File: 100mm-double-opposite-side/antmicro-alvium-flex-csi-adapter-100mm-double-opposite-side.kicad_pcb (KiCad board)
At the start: 2 copper layers, 81.8 x 100.1 mm, 3 parts, among them J1 WE_687622100002_FLEX, J2 WE_687622100002_FLEX, J3 WE_687650100002_FLEX

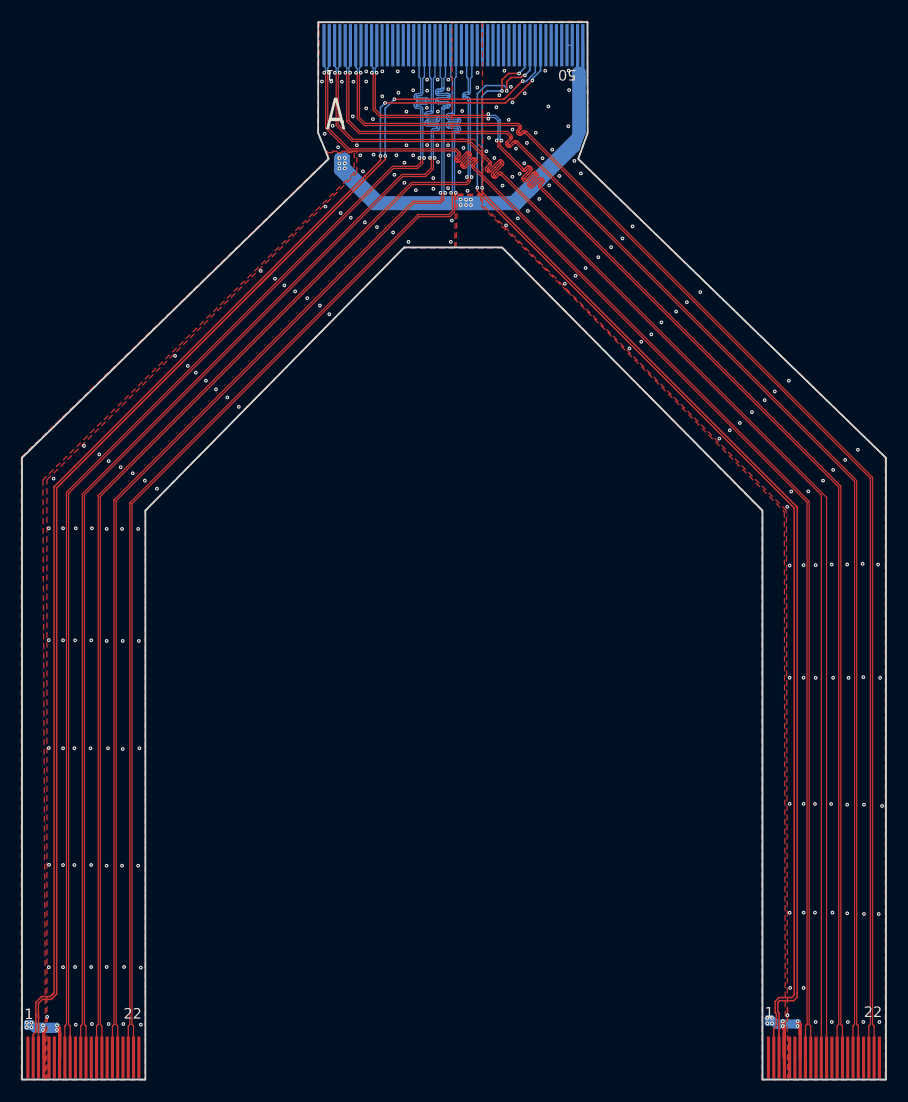
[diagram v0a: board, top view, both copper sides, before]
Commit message: 100mm-double-opposite: tweak polygon pours
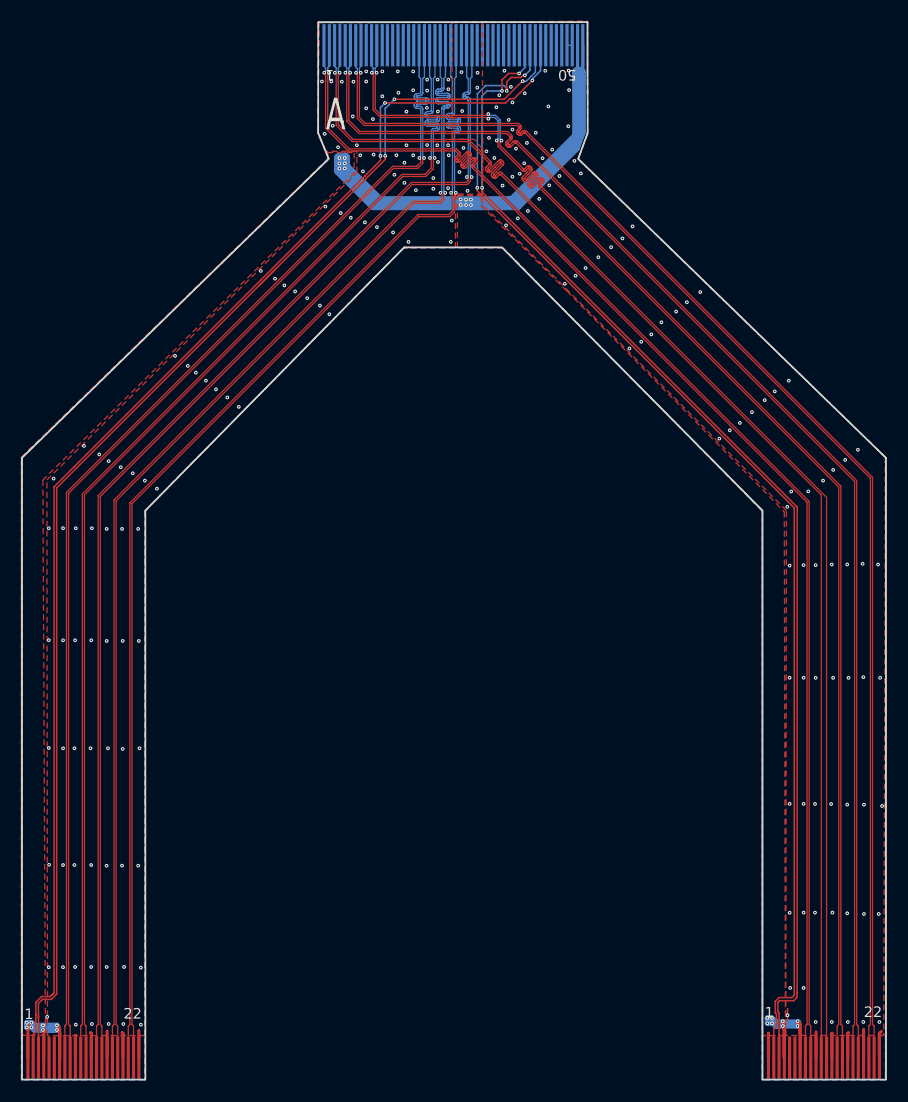
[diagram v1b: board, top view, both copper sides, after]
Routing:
- net /F1_GND: track 1.53 -> 25.9 mm
- net /F1_5V: track 115.4 -> 120.8 mm
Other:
- board text added: "Stiffener TOP"
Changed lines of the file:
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@@
-(kicad_pcb (version 20171130) (host pcbnew 5.1.6)
+(kicad_pcb (version 20171130) (host pcbnew 5.1.5+dfsg1-2~bpo10+1)
   (general
     (thickness 1.6)
     (drawings 73)
-    (tracks 1988)
+    (tracks 2008)
     (zones 0)
     (modules 3)
@@
   (page A4)
   (layers
-    (0 F.Cu signal)
-    (31 B.Cu signal)
+    (0 F.Cu signal hide)
+    (31 B.Cu signal hide)
     (32 B.Adhes user hide)
     (33 F.Adhes user hide)
     (34 B.Paste user hide)
     (35 F.Paste user hide)
-    (36 B.SilkS user)
-    (37 F.SilkS user)
+    (36 B.SilkS user hide)
+    (37 F.SilkS user hide)
     (38 B.Mask user hide)
     (39 F.Mask user hide)
-    (40 Dwgs.User user)
-    (41 Cmts.User user)
-    (42 Eco1.User user)
-    (43 Eco2.User user)
+    (40 Dwgs.User user hide)
+    (41 Cmts.User user hide)
+    (42 Eco1.User user hide)
+    (43 Eco2.User user hide)
     (44 Edge.Cuts user)
-    (45 Margin user)
-    (46 B.CrtYd user)
-    (47 F.CrtYd user)
-    (48 B.Fab user)
+    (45 Margin user hide)
+    (46 B.CrtYd user hide)
+    (47 F.CrtYd user hide)
+    (48 B.Fab user hide)
     (49 F.Fab user)
   )
   (setup
-    (last_trace_width 0.1)
+    (last_trace_width 0.3)
     (user_trace_width 0.1)
     (user_trace_width 0.15)
@@
   (gr_line (start 152.313 118.802) (end 163.997 118.802) (layer B.Fab) (width 0.15))
   (gr_line (start 82.209 111.662) (end 93.893 111.662) (layer B.Fab) (width 0.15))
-  (gr_text "Stiffener BOTTOM" (at 102.57 24.662) (layer B.Fab)
+  (gr_text "Stiffener TOP" (at 123.56 21.41) (layer F.Fab)
     (effects (font (size 1 1) (thickness 0.15)))
   )
@@
   (segment (start 154.686 112.164) (end 154.686 112.776) (width 0.15) (layer F.Cu) (net 1))
   (segment (start 154.7 112.15) (end 154.686 112.164) (width 0.15) (layer F.Cu) (net 1))
+  (segment (start 87.2824 114.689198) (end 87.29 114.681598) (width 0.3) (layer F.Cu) (net 1))
+  (segment (start 87.2824 116.7892) (end 87.2824 114.689198) (width 0.3) (layer F.Cu) (net 1))
+  (segment (start 88.7824 114.4892) (end 88.71 114.4168) (width 0.3) (layer F.Cu) (net 1))
+  (segment (start 88.7824 116.7892) (end 88.7824 114.4892) (width 0.3) (layer F.Cu) (net 1))
+  (segment (start 90.2824 116.7892) (end 90.2824 114.2724) (width 0.3) (layer F.Cu) (net 1))
+  (segment (start 91.7824 114.4892) (end 91.7 114.4068) (width 0.3) (layer F.Cu) (net 1))
+  (segment (start 91.7824 116.7892) (end 91.7824 114.4892) (width 0.3) (layer F.Cu) (net 1))
+  (segment (start 93.2824 116.7892) (end 93.2824 114.2176) (width 0.3) (layer F.Cu) (net 1))
+  (segment (start 157.3864 116.79) (end 157.3864 114.3464) (width 0.3) (layer F.Cu) (net 1))
+  (segment (start 158.8864 114.49) (end 158.9 114.4764) (width 0.3) (layer F.Cu) (net 1))
+  (segment (start 158.8864 116.79) (end 158.8864 114.49) (width 0.3) (layer F.Cu) (net 1))
+  (segment (start 160.3864 114.49) (end 160.45 114.4264) (width 0.3) (layer F.Cu) (net 1))
+  (segment (start 160.3864 116.79) (end 160.3864 114.49) (width 0.3) (layer F.Cu) (net 1))
+  (segment (start 161.8864 116.79) (end 161.8864 114.1164) (width 0.3) (layer F.Cu) (net 1))
+  (segment (start 163.3864 114.49) (end 163.57 114.3064) (width 0.3) (layer F.Cu) (net 1))
+  (segment (start 163.3864 116.79) (end 163.3864 114.49) (width 0.3) (layer F.Cu) (net 1))
   (segment (start 162.8864 116.79) (end 162.8864 113.78959) (width 0.1) (layer F.Cu) (net 2))
   (segment (start 129.255204 29.157372) (end 129.255204 29.129381) (width 0.1) (layer F.Cu) (net 2))
@@
   (segment (start 135.313 23.26999) (end 135.08799 23.495) (width 0.3) (layer B.Cu) (net 12))
   (segment (start 135.313 20.955) (end 135.313 23.26999) (width 0.3) (layer B.Cu) (net 12))
+  (segment (start 82.7824 113.8136) (end 82.88 113.716) (width 0.2) (layer F.Cu) (net 12))
+  (segment (start 82.7824 116.7892) (end 82.7824 113.8136) (width 0.3) (layer F.Cu) (net 12))
+  (segment (start 152.8864 114.49) (end 152.88 114.4836) (width 0.3) (layer F.Cu) (net 12))
+  (segment (start 152.8864 116.79) (end 152.8864 114.49) (width 0.3) (layer F.Cu) (net 12))
   (segment (start 155.6004 110.744) (end 155.6004 110.617) (width 0.15) (layer F.Cu) (net 13))
   (via (at 125.773603 34.4424) (size 0.35) (drill 0.15) (layers F.Cu B.Cu) (net 13))
@@
     (polygon
       (pts
-        (xy 125.6792 36.1188) (xy 133.82625 44.243625) (xy 154.384375 65.103375) (xy 154.479625 118.872) (xy 152.273 118.872)
-        (xy 152.273 65.024) (xy 127.762 40.132) (xy 123.317 40.132) (xy 123.444 35.179) (xy 125.6665 35.179)
+        (xy 125.6792 36.1188) (xy 133.82625 44.243625) (xy 154.384375 65.103375) (xy 154.489602 114.7) (xy 152.290399 114.7)
+        (xy 152.273 65.024) (xy 127.762 40.132) (xy 123.44 40.09) (xy 123.444 35.179) (xy 125.6665 35.179)
       )
     )
@@
     (polygon
       (pts
-        (xy 125.857 35.052) (xy 123.2535 35.052) (xy 123.19 40.132) (xy 118.364 40.132) (xy 93.853 65.024)
-        (xy 93.853 118.872) (xy 84.582 118.872) (xy 84.582 62.103) (xy 113.919 33.02) (xy 113.919 30.988)
+        (xy 125.857 35.052) (xy 123.2535 35.052) (xy 123.25 40.08) (xy 118.364 40.132) (xy 93.853 65.024)
+        (xy 93.9055 114.7) (xy 84.6345 114.7) (xy 84.582 62.103) (xy 113.919 33.02) (xy 113.919 30.988)
         (xy 110.998 30.988) (xy 110.236 29.21) (xy 110.363 18.796) (xy 125.7935 18.796)
       )
@@
     (polygon
       (pts
-        (xy 113.665 33.02) (xy 84.201 62.103) (xy 84.455 118.872) (xy 82.169 118.872) (xy 82.169 59.944)
+        (xy 113.665 33.02) (xy 84.201 62.103) (xy 84.443 114.67) (xy 82.157 114.67) (xy 82.169 59.944)
         (xy 111.252 31.623) (xy 111.125 31.115) (xy 113.665 31.115)
       )
@@
     (polygon
       (pts
-        (xy 135.763 29.21) (xy 134.874 31.75) (xy 163.957 59.944) (xy 163.957 118.872) (xy 154.686 118.872)
+        (xy 135.763 29.21) (xy 134.874 31.75) (xy 163.957 59.944) (xy 163.795657 114.69) (xy 154.524344 114.69)
         (xy 154.5844 64.9986) (xy 125.8062 36.0172) (xy 125.7808 30.734) (xy 125.0315 29.845) (xy 122.936 29.845)
         (xy 122.936 18.796) (xy 135.763 18.669)

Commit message: 100mm-double-opposite: Add signage
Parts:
- added N1: oshw_logo, antmicro-footprints:oshw-logo, B.Cu at (87.7, 93.1)
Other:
- board text added: "Antmicro Alvium Flex CSI Adapter 100mm double opposite contacts Rev. 1.0.0"
- board text added: "LED ->"
- board text removed: "A"

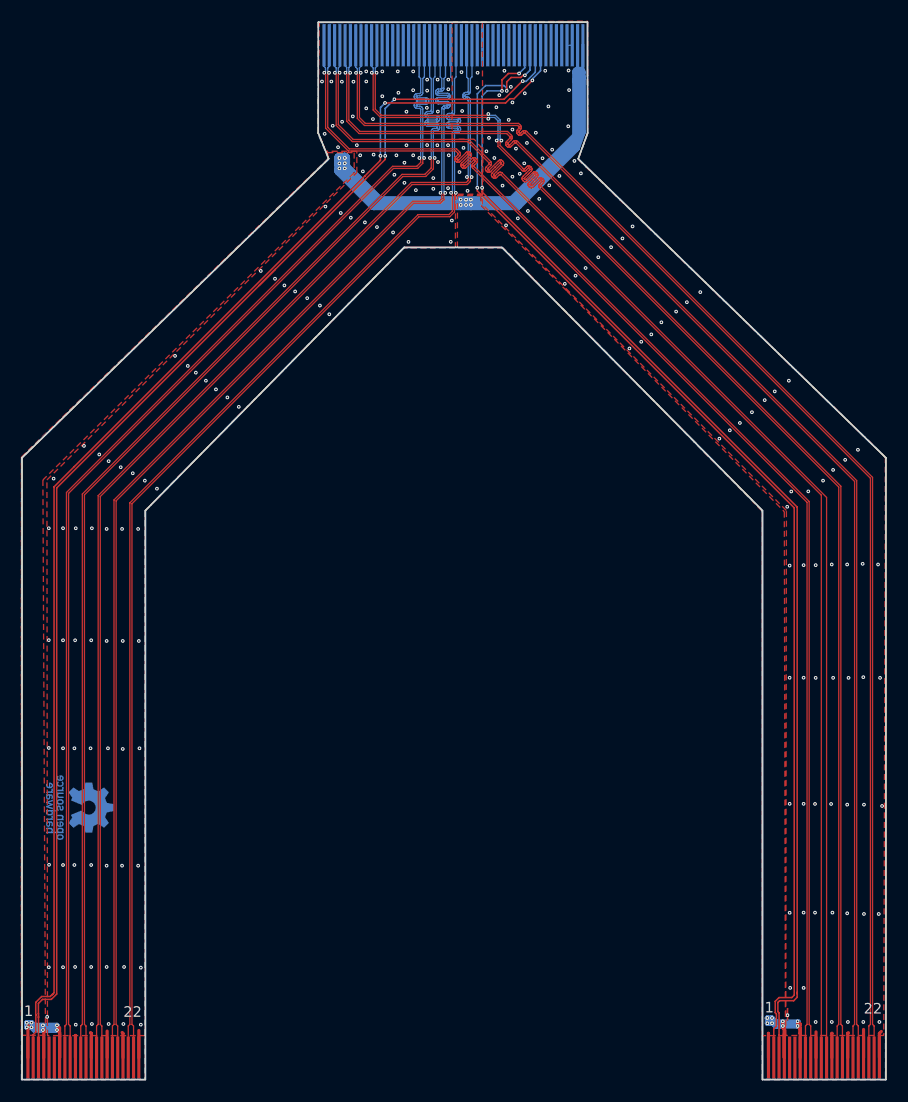
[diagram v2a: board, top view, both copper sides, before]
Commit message: 100mm-double-opposite: update OSHW logotype
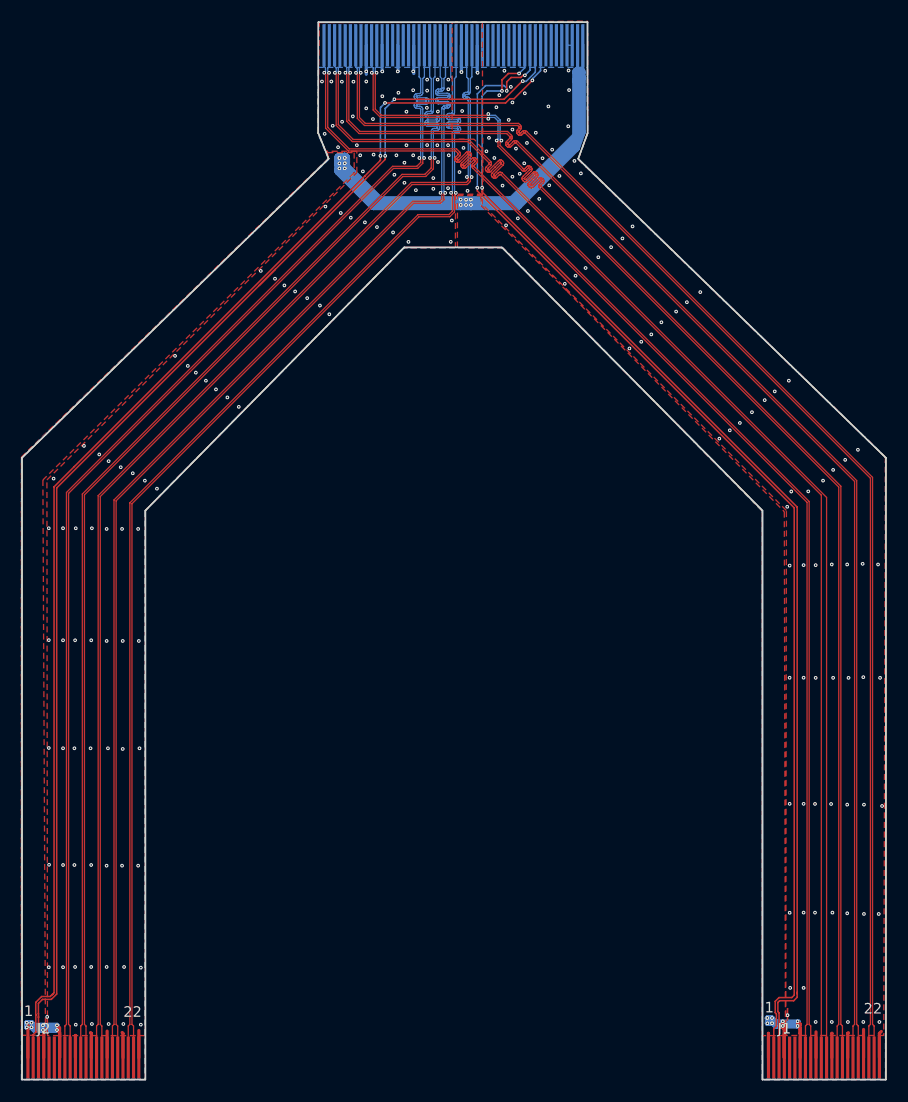
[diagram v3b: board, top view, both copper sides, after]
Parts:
- N1: footprint antmicro-footprints:oshw-logo -> antmicro-alvium-flex-csi-adapter-footprints:oshw-logo
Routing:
- net /F1_GND: track 25.9 -> 41.5 mm
